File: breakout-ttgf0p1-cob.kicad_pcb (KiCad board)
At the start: 2 copper layers, 71.3 x 71.3 mm, 10 parts, among them J1 Conn_02x05_Odd_Even, J2 Conn_02x08_Odd_Even, J3 Conn_02x05_Odd_Even, J4 Conn_02x08_Odd_Even, J5 Conn_02x05_Odd_Even, J6 Conn_02x08_Odd_Even, J7 Conn_02x05_Odd_Even, J8 Conn_02x08_Odd_Even, U1 TTGF0p1

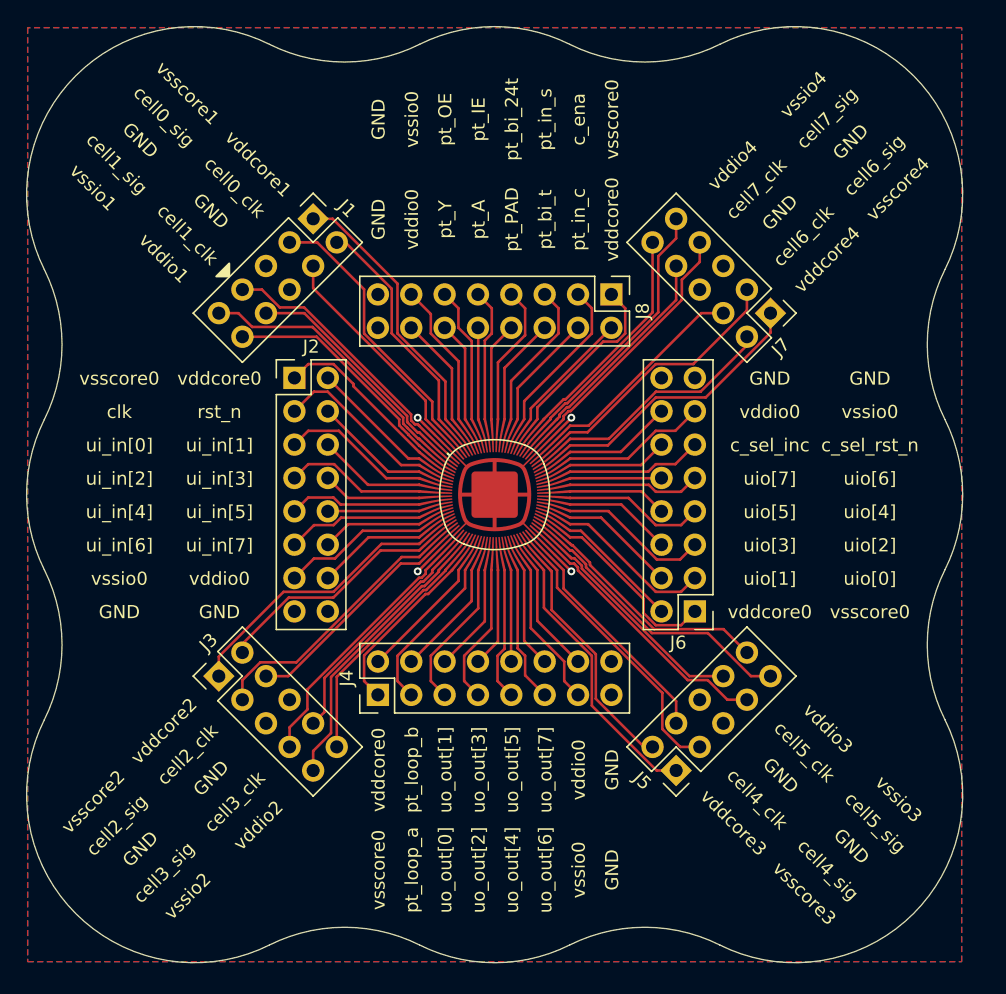
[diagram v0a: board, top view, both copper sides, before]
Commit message: add some silkscreen
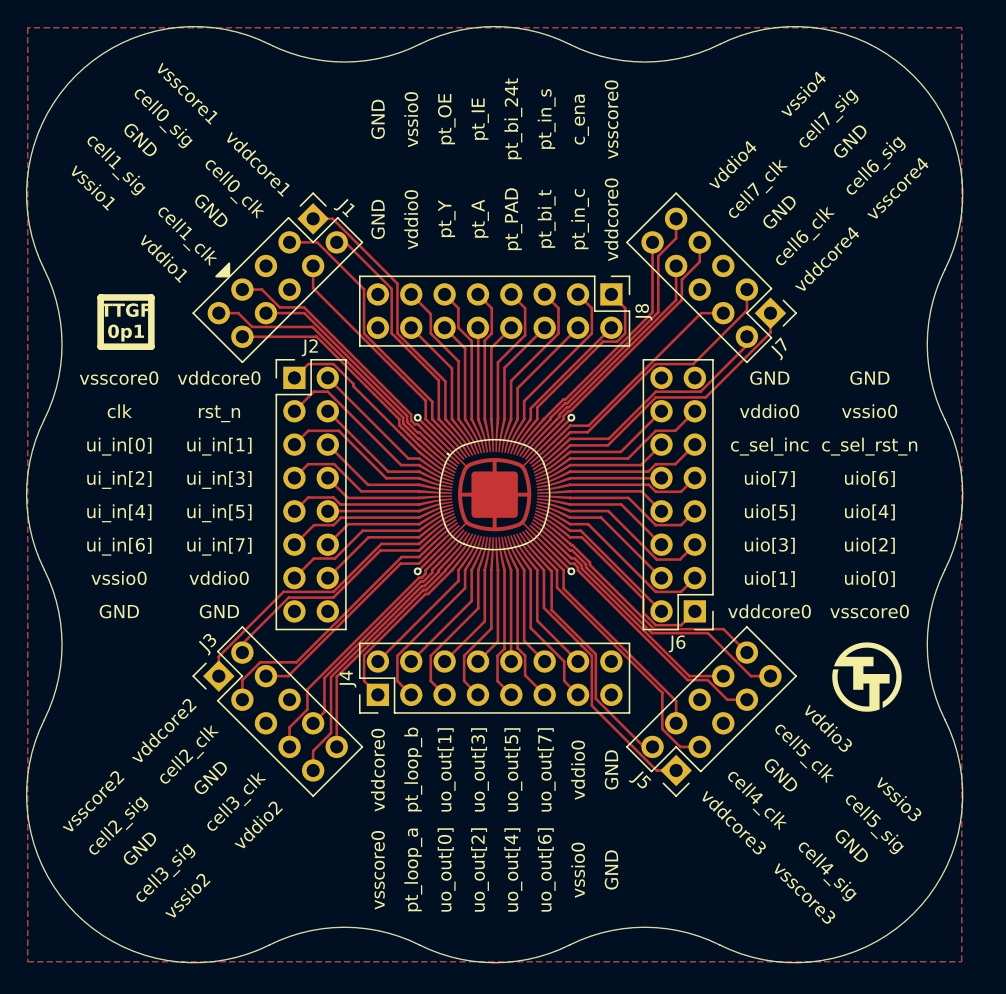
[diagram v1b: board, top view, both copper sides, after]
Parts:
- added TTLOGO1: TT_logo, Logos:TT_logo, F.Cu at (178.3, 113.0)
- added TTLOGO1: TT_logo, Logos:TT_logo, B.Cu at (150.1, 99.1)
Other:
- board text added: "TTGF 0p1"
- board text added: "tinytapeout.com"

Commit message: rotate cob pcb to match adapter board
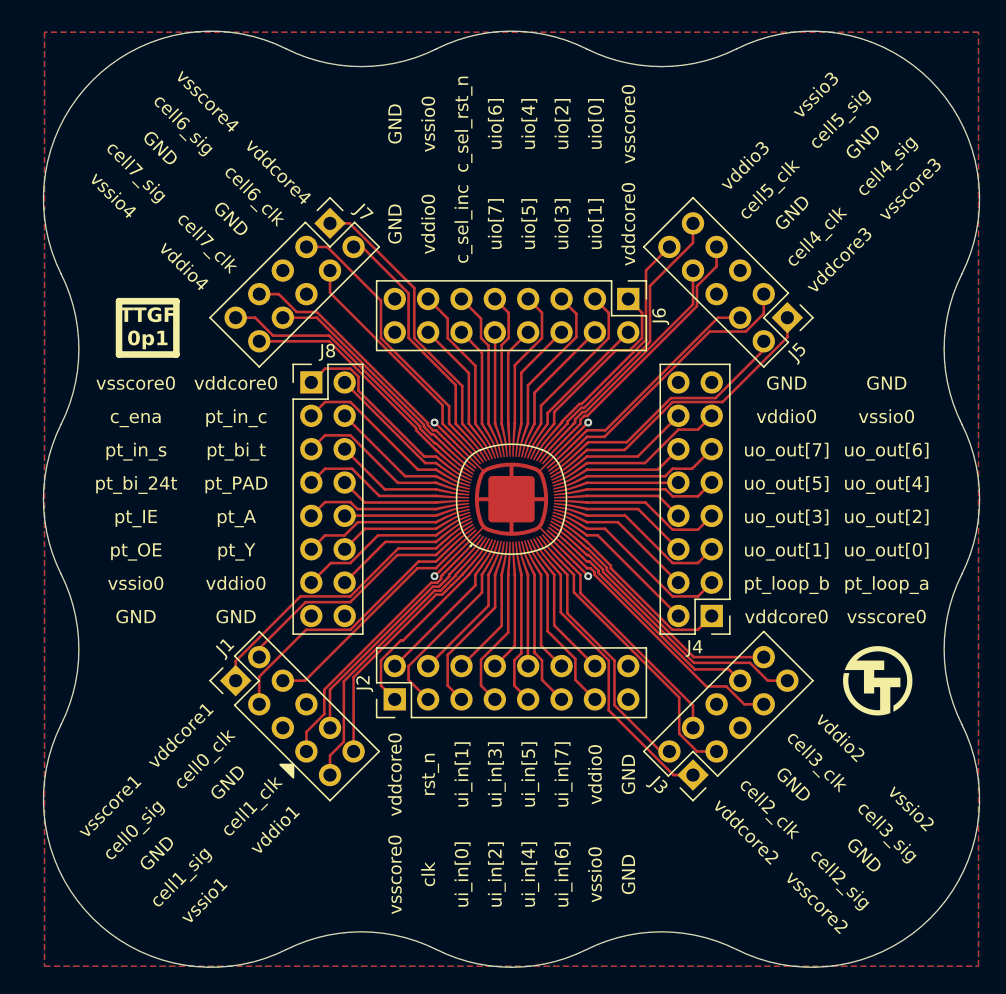
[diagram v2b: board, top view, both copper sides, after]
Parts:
- moved J3 36.9 mm to (165.0, 120.4), turned to 135 degrees
- moved J1 35.7 mm to (130.1, 113.2), turned to 45 degrees
- moved J5 35.5 mm to (172.1, 85.6), turned to -135 degrees
- moved J7 34.2 mm to (137.3, 78.4), turned to -45 degrees
- moved J4 26.1 mm to (166.4, 108.3), turned to 180 degrees
- moved J2 25.6 mm to (142.3, 114.7), turned to 90 degrees
- moved J6 24.3 mm to (160.0, 84.2), turned to -90 degrees
- moved J8 23.8 mm to (135.9, 90.5), turned to 0 degrees
- moved ? 11.5 mm to (145.9, 105.2), turned to 90 degrees
- moved U1 1.33 mm to (151.1, 99.4), turned to 90 degrees
- moved TTLOGO1 1.02 mm to (151.1, 99.1)
- moved TTLOGO1 0.87 mm to (179.1, 113.3)

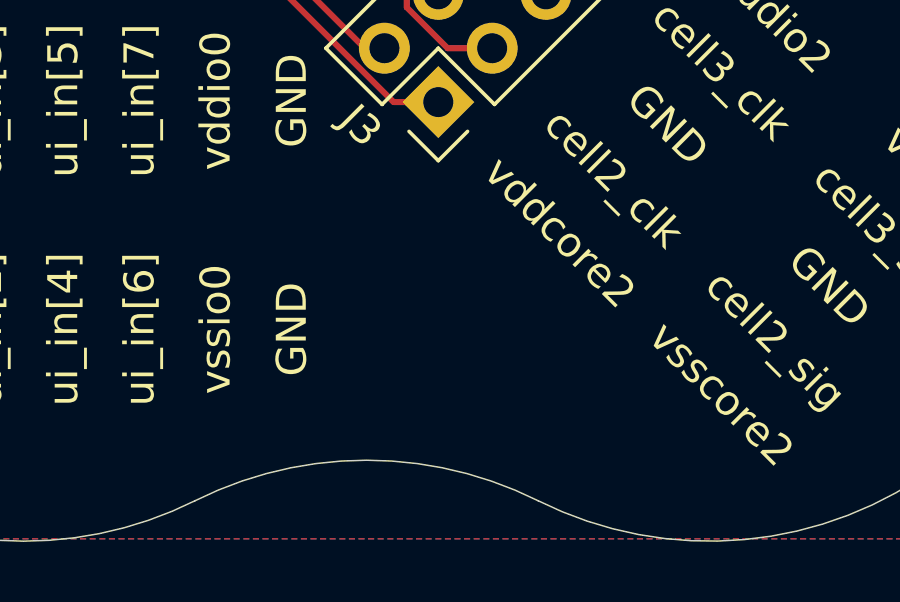
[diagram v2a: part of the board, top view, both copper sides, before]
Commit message: add tillitis logo
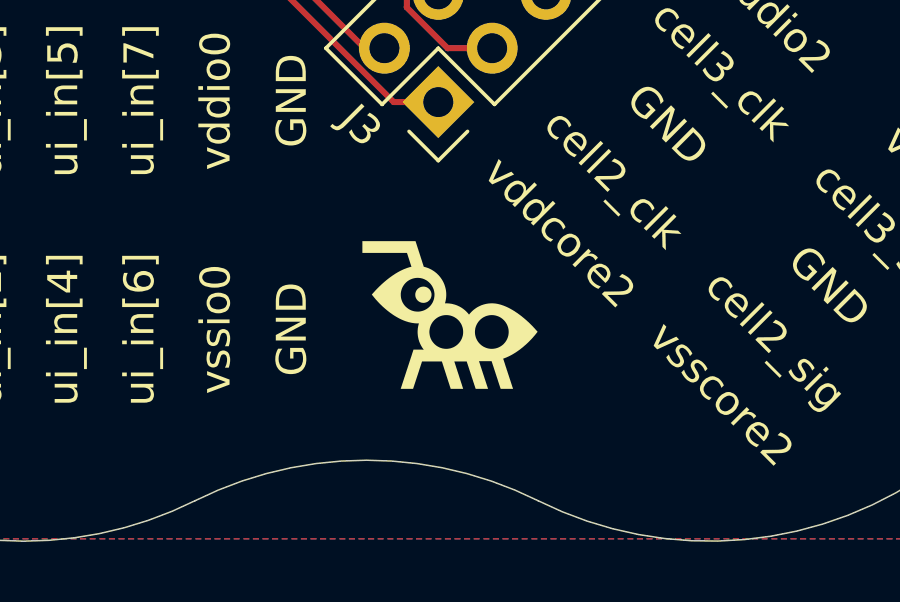
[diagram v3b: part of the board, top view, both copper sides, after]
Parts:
- added TILL1: Tillitis_logo, Logos:tillitis_logo, F.Cu at (165.4, 127.5)
